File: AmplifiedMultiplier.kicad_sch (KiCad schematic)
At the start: 30 parts, among them IC1 AD835ARZ, J11 SMA, J13 RFShield_OnePiece, J14 RFShield_OnePiece, J15 u.fl, J17 SMA, T1 MABA-007532-CF18A0, T2 MABA-007532-CF18A0

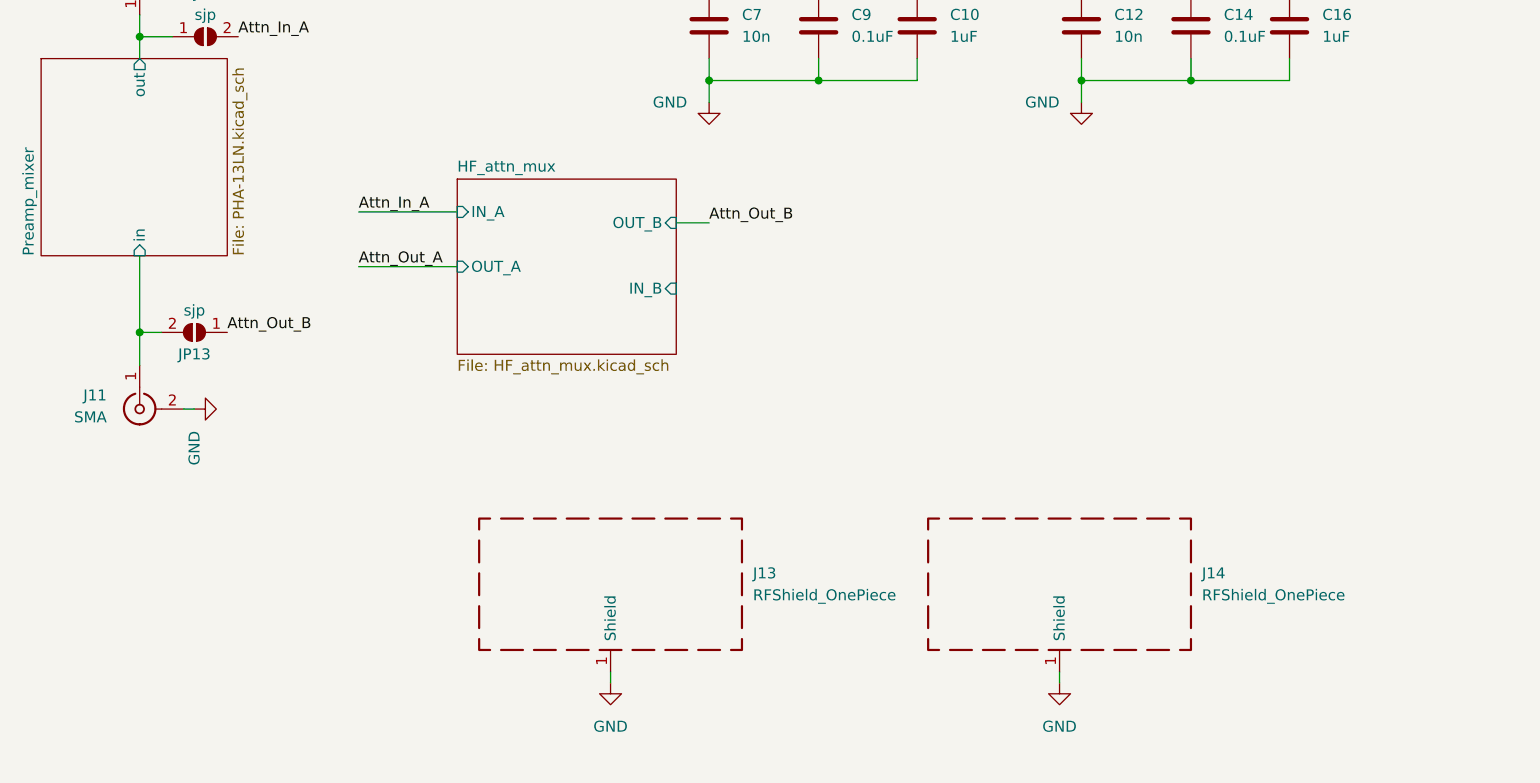
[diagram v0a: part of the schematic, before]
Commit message: Digital section half finished
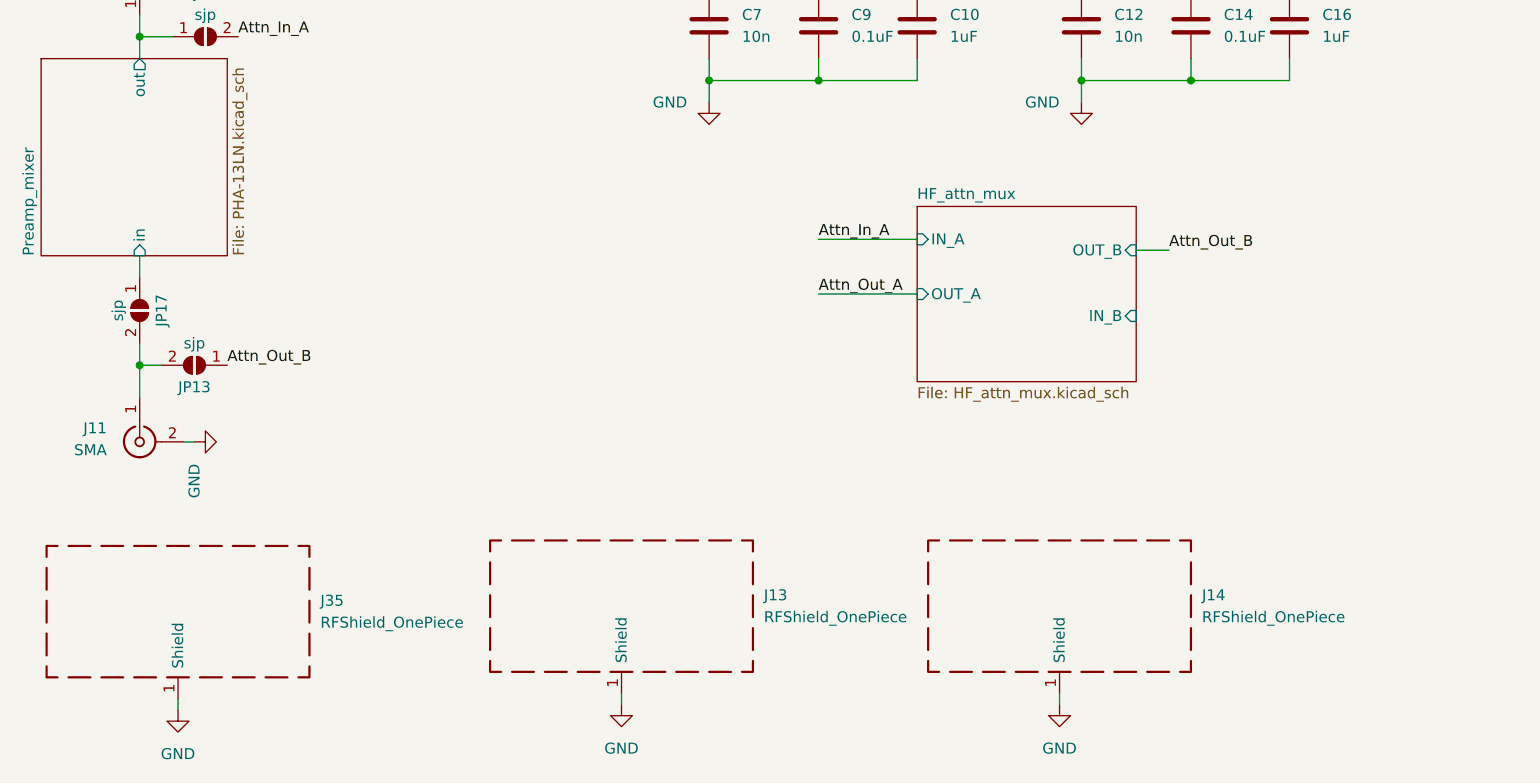
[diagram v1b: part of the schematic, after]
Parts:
- added J35: RFShield_OnePiece, SamacSys_Parts:21187222_RF_shield, symbol Device:RFShield_OnePiece
- added JP17: sjp, Jumper:SolderJumper-2_P1.3mm_Open_RoundedPad1.0x1.5mm, symbol Jumper:SolderJumper_2_Open
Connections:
- net GND: now also J35.1 (Shield)
- net Preamp_mixer/in: now also JP17.1 (A); no longer J11.1 (In), JP13.2 (B)
- new net: J11.1 (In), JP13.2 (B), JP17.2 (B)
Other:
- moved on the sheet: J11, J13, J14, JP13

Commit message: First finished draft
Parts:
- added R178: 1k, Resistor_SMD:R_0805_2012Metric, symbol Device:R
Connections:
- net at J11.1 (In), JP13.2 (B), JP17.2 (B): now also R178.2
- new net reflection_DC: R178.1
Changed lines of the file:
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@@
+    (stroke (width 0) (type default) (color 0 0 0 0))
+  )
+  (wire (pts (xy 19.05 153.67) (xy 19.05 151.13))
     (stroke (width 0) (type default) (color 0 0 0 0))
   )
@@
     (stroke (width 0) (type default) (color 0 0 0 0))
   )
+  (wire (pts (xy 19.05 151.13) (xy 22.86 151.13))
+    (stroke (width 0) (type default) (color 0 0 0 0))
+  )
   (wire (pts (xy 229.87 146.05) (xy 231.14 146.05))
     (stroke (width 0) (type default) (color 0 0 0 0))
@@
   )
   (wire (pts (xy 95.25 58.42) (xy 96.52 58.42))
+    (stroke (width 0) (type default) (color 0 0 0 0))
+  )
+  (wire (pts (xy 30.48 151.13) (xy 34.29 151.13))
     (stroke (width 0) (type default) (color 0 0 0 0))
   )
@@
     )
   )
+  (global_label "reflection_DC" (shape input) (at 19.05 153.67 270) (fields_autoplaced)
+    (effects (font (size 1.27 1.27)) (justify right))
+    (property "Intersheet References" "${INTERSHEET_REFS}" (id 0) (at 18.9706 168.6621 90)
+      (effects (font (size 1.27 1.27)) (justify right) hide)
+    )
+  )
   (symbol (lib_id "Device:C") (at 113.03 58.42 180) (unit 1)
     (in_bom yes) (on_board yes) (fields_autoplaced)
@@
       (effects (font (size 1.27 1.27)) hide)
     )
+    (pin "1")
+    (pin "2")
+  )
+  (symbol (lib_id "Device:R") (at 26.67 151.13 90) (unit 1)
+    (in_bom yes) (on_board yes) (fields_autoplaced)
+    (property "Reference" "R178" (id 0) (at 26.67 144.78 90))
+    (property "Value" "1k" (id 1) (at 26.67 147.32 90))
+    (property "Footprint" "Resistor_SMD:R_0805_2012Metric" (id 2) (at 26.67 152.908 90)
+      (effects (font (size 1.27 1.27)) hide)
+    )
+    (property "Datasheet" "~" (id 3) (at 26.67 151.13 0)
+      (effects (font (size 1.27 1.27)) hide)
+    )

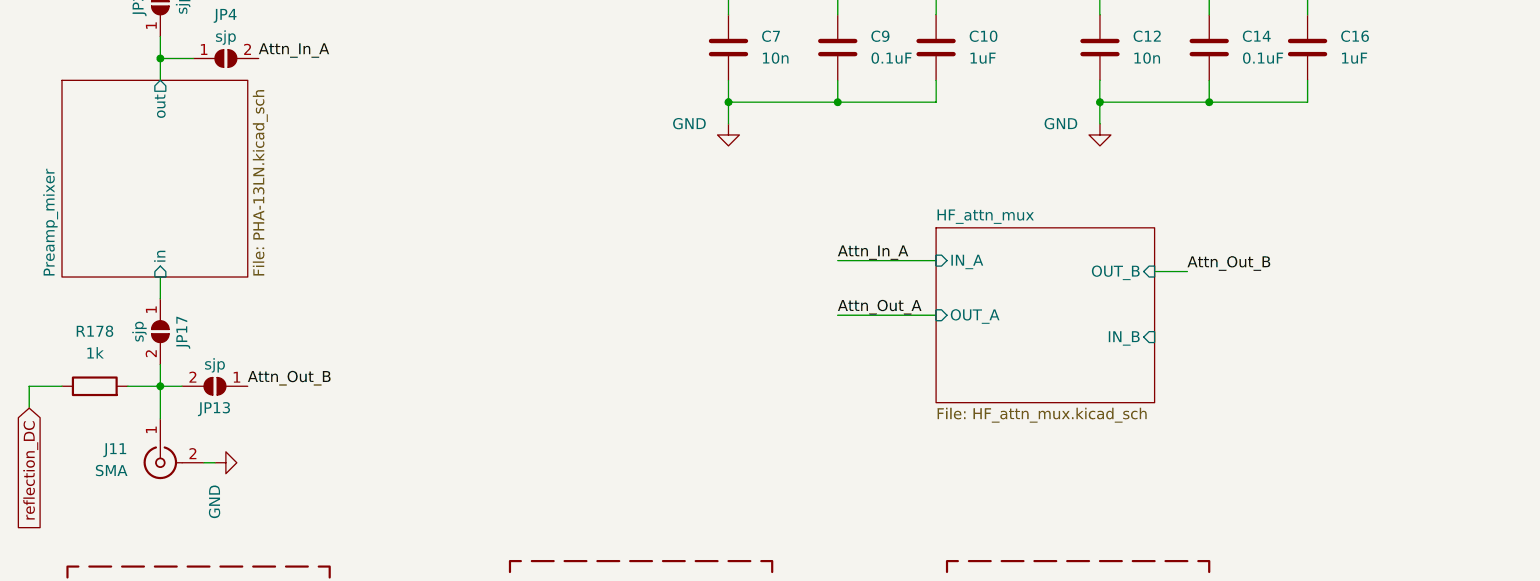
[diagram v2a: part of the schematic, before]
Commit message: First finished version. Still need to check some footprint for critical parts and also refine the part numbers before order
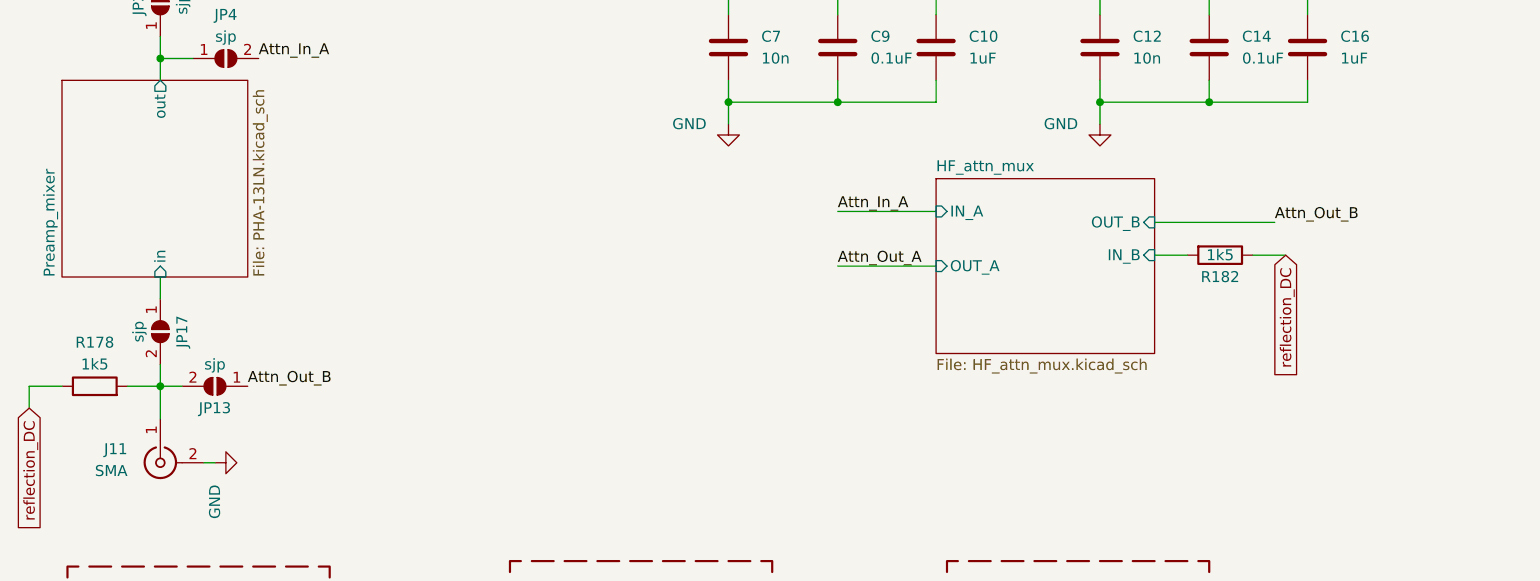
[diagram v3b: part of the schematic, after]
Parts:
- added R182: 1k5, Resistor_SMD:R_0805_2012Metric, symbol Device:R
- R178: value 1k -> 1k5
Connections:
- net HF_attn_mux/IN_B: now also R182.2
- net reflection_DC: now also R182.1
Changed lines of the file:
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@@
     (stroke (width 0) (type default) (color 0 0 0 0))
   )
-  (wire (pts (xy 153.67 137.795) (xy 149.86 137.795))
+  (wire (pts (xy 163.83 132.08) (xy 149.86 132.08))
     (stroke (width 0) (type default) (color 0 0 0 0))
   )
@@
     (stroke (width 0) (type default) (color 0 0 0 0))
   )
-  (wire (pts (xy 113.03 142.875) (xy 124.46 142.875))
+  (wire (pts (xy 113.03 137.16) (xy 124.46 137.16))
     (stroke (width 0) (type default) (color 0 0 0 0))
   )
@@
     (stroke (width 0) (type default) (color 0 0 0 0))
   )
+  (wire (pts (xy 153.67 135.89) (xy 149.86 135.89))
+    (stroke (width 0) (type default) (color 0 0 0 0))
+  )
   (wire (pts (xy 163.83 54.61) (xy 163.83 50.8))
     (stroke (width 0) (type default) (color 0 0 0 0))
@@
     (stroke (width 0) (type default) (color 0 0 0 0))
   )
+  (wire (pts (xy 165.1 135.89) (xy 161.29 135.89))
+    (stroke (width 0) (type default) (color 0 0 0 0))
+  )
   (wire (pts (xy 156.21 115.57) (xy 156.21 118.11))
     (stroke (width 0) (type default) (color 0 0 0 0))
@@
     (stroke (width 0) (type default) (color 0 0 0 0))
   )
-  (wire (pts (xy 113.03 136.525) (xy 124.46 136.525))
+  (wire (pts (xy 113.03 130.81) (xy 124.46 130.81))
     (stroke (width 0) (type default) (color 0 0 0 0))
   )
@@
     (stroke (width 0) (type default) (color 0 0 0 0))
   )
-  (label "Attn_In_A" (at 113.03 136.525 0)
+  (label "Attn_In_A" (at 113.03 130.81 0)
     (effects (font (size 1.27 1.27)) (justify left bottom))
   )
@@
     (effects (font (size 1.27 1.27)) (justify left bottom))
   )
-  (label "Attn_Out_B" (at 153.67 137.795 0)
+  (label "Attn_Out_B" (at 163.83 132.08 0)
     (effects (font (size 1.27 1.27)) (justify left bottom))
   )
-  (label "Attn_Out_A" (at 113.03 142.875 0)
+  (label "Attn_Out_A" (at 113.03 137.16 0)
     (effects (font (size 1.27 1.27)) (justify left bottom))
   )
@@
     )
   )
+  (global_label "reflection_DC" (shape input) (at 165.1 135.89 270) (fields_autoplaced)
+    (effects (font (size 1.27 1.27)) (justify right))
+    (property "Intersheet References" "${INTERSHEET_REFS}" (id 0) (at 165.1794 150.8821 90)
+      (effects (font (size 1.27 1.27)) (justify left) hide)
+    )
+  )
   (symbol (lib_id "Device:C") (at 113.03 58.42 180) (unit 1)
     (in_bom yes) (on_board yes) (fields_autoplaced)
@@
   )
   (symbol (lib_id "Device:R") (at 26.67 151.13 90) (unit 1)
-    (in_bom yes) (on_board yes) (fields_autoplaced)
-    (property "Reference" "R178" (id 0) (at 26.67 144.78 90))
-    (property "Value" "1k" (id 1) (at 26.67 147.32 90))
+    (in_bom yes) (on_board yes)
+    (property "Reference" "R178" (id 0) (at 26.67 146.05 90))
+    (property "Value" "1k5" (id 1) (at 26.67 148.59 90))
     (property "Footprint" "Resistor_SMD:R_0805_2012Metric" (id 2) (at 26.67 152.908 90)
       (effects (font (size 1.27 1.27)) hide)
@@
     )
     (property "Datasheet" " ~" (id 3) (at 236.22 146.05 0)
+      (effects (font (size 1.27 1.27)) hide)
+    )
+    (pin "1")
+    (pin "2")
+  )
+  (symbol (lib_id "Device:R") (at 157.48 135.89 270) (unit 1)
+    (in_bom yes) (on_board yes)
+    (property "Reference" "R182" (id 0) (at 157.48 138.43 90))
+    (property "Value" "1k5" (id 1) (at 157.48 135.89 90))
+    (property "Footprint" "Resistor_SMD:R_0805_2012Metric" (id 2) (at 157.48 134.112 90)
+      (effects (font (size 1.27 1.27)) hide)
+    )
+    (property "Datasheet" "~" (id 3) (at 157.48 135.89 0)
       (effects (font (size 1.27 1.27)) hide)
     )
@@
     )
   )
-  (sheet (at 124.46 132.715) (size 25.4 20.32) (fields_autoplaced)
+  (sheet (at 124.46 127) (size 25.4 20.32) (fields_autoplaced)
     (stroke (width 0.1524) (type solid) (color 0 0 0 0))
     (fill (color 0 0 0 0.0000))
-    (property "Sheet name" "HF_attn_mux" (id 0) (at 124.46 132.0034 0)
+    (property "Sheet name" "HF_attn_mux" (id 0) (at 124.46 126.2884 0)
       (effects (font (size 1.27 1.27)) (justify left bottom))
     )
-    (property "Sheet file" "HF_attn_mux.kicad_sch" (id 1) (at 124.46 153.6196 0)
+    (property "Sheet file" "HF_attn_mux.kicad_sch" (id 1) (at 124.46 147.9046 0)
       (effects (font (size 1.27 1.27)) (justify left top))
     )
-    (pin "IN_A" input (at 124.46 136.525 180)
-      (effects (font (size 1.27 1.27)) (justify left))
-    )
-    (pin "OUT_B" input (at 149.86 137.795 0)
-      (effects (font (size 1.27 1.27)) (justify right))
-    )
-    (pin "OUT_A" input (at 124.46 142.875 180)
-      (effects (font (size 1.27 1.27)) (justify left))
-    )
-    (pin "IN_B" input (at 149.86 145.415 0)
-      (effects (font (size 1.27 1.27)) (justify right))
-    )
+    (pin "IN_A" input (at 124.46 130.81 180)
+      (effects (font (size 1.27 1.27)) (justify left))
+    )
+    (pin "OUT_B" input (at 149.86 132.08 0)
+      (effects (font (size 1.27 1.27)) (justify right))
+    )
+    (pin "OUT_A" input (at 124.46 137.16 180)
+      (effects (font (size 1.27 1.27)) (justify left))
+    )
+    (pin "IN_B" input (at 149.86 135.89 0)
+      (effects (font (size 1.27 1.27)) (justify right))
+    )
